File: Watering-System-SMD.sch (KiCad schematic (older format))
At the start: 21 parts, among them CON1 AVR-ISP-6, J1 Screw_Terminal_1x02, J2 CONN_01X04_MALE, J3 Screw_Terminal_1x04, J4 Screw_Terminal_1x02, Q1 MMBF170, Q2 2N7002, U1 MCP1703A-3302/MB, U2 ATTINY84-20SSU, U3 ESP-01

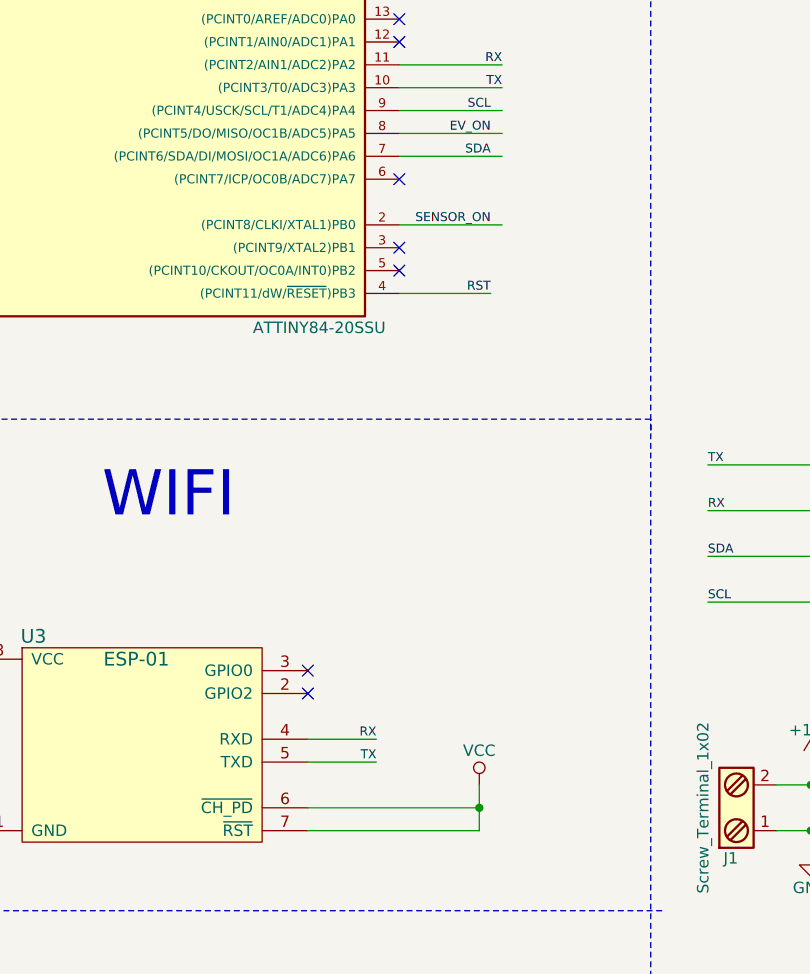
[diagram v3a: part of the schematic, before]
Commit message: CH-PD routed
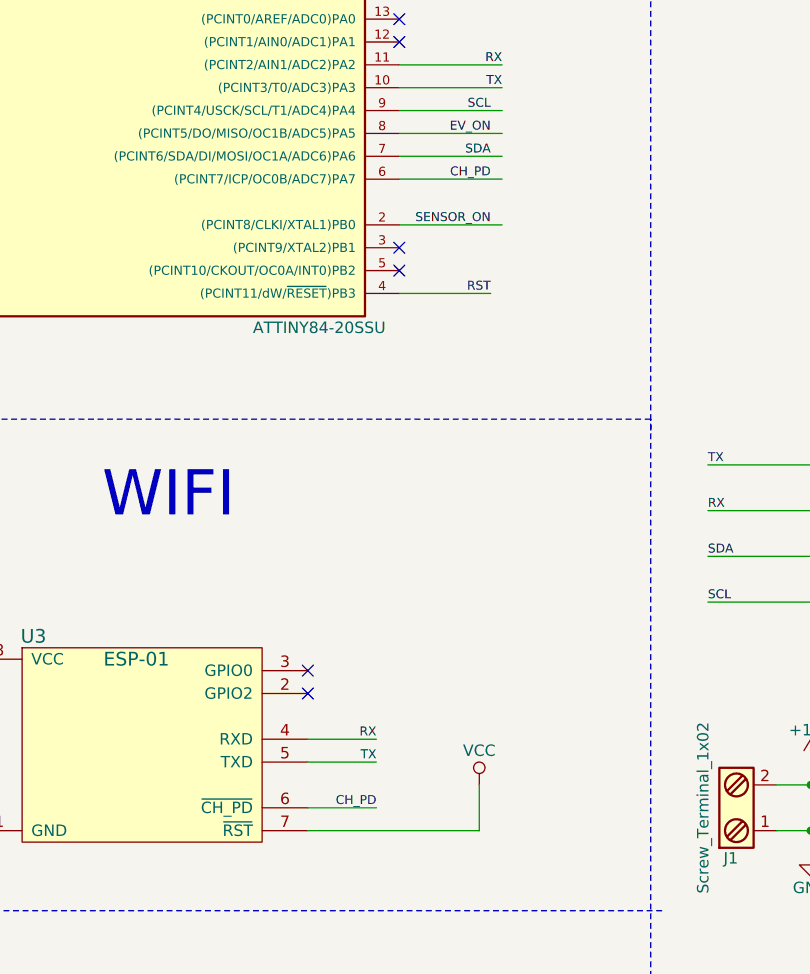
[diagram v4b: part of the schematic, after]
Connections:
- net labels added: CH_PD
- wire segments 78 -> 79
- no-connect marks 7 -> 6
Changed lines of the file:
@@
 Text Label 7000 1400 2    39   ~ 0
 RX
-NoConn ~ 6550 1900
 NoConn ~ 6550 2200
 NoConn ~ 6550 2300
@@
 	6150 4450 6450 4450
 Wire Wire Line
-	6150 4650 6900 4650
-Wire Wire Line
 	6900 4550 6900 4750
 Wire Wire Line
 	6900 4750 6150 4750
-Connection ~ 6900 4650
 $Comp
 L VCC #PWR021
@@
 Wire Wire Line
 	4600 4750 4600 4850
+Wire Wire Line
+	6150 4650 6450 4650
+Wire Wire Line
+	6550 1900 7000 1900
+Text Label 6950 1900 2    39   ~ 0
+CH_PD
+Text Label 6450 4650 2    39   ~ 0
+CH_PD
 $EndSCHEMATC

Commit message: MOSFET transistor changed
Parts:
- Q1: symbol MMBF170 -> MMBF170-RESCUE-Watering-System-SMD
- Q2: symbol 2N7002 -> 2N7002-RESCUE-Watering-System-SMD
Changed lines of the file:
@@
 EESchema Schematic File Version 2
+LIBS:Watering-System-SMD-rescue
 LIBS:power
 LIBS:device
@@
 $EndComp
 $Comp
-L MMBF170 Q1
+L MMBF170-RESCUE-Watering-System-SMD Q1
 U 1 1 5923371B
 P 2650 6950
@@
 $EndComp
 $Comp
-L 2N7002 Q2
+L 2N7002-RESCUE-Watering-System-SMD Q2
 U 1 1 592337CE
 P 5300 6800

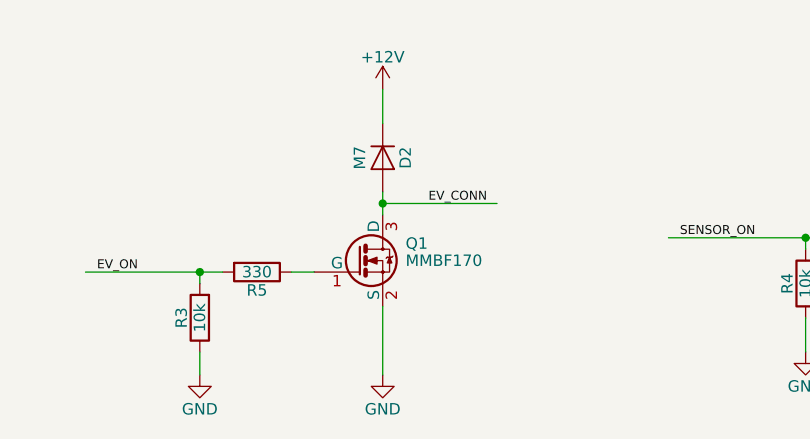
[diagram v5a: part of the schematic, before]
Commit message: MOSFET changed
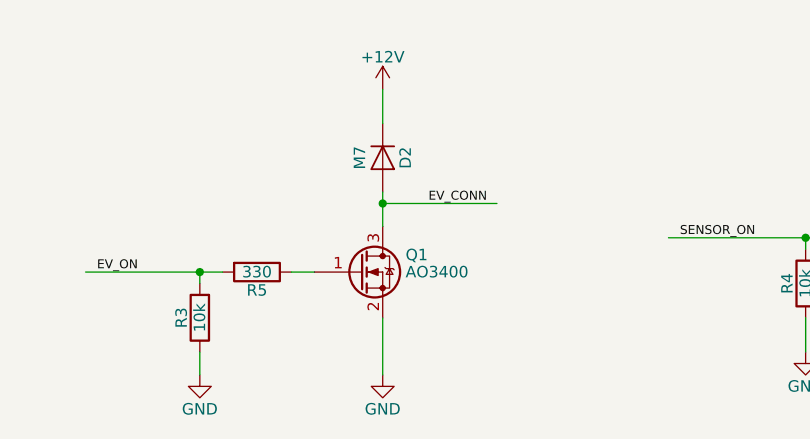
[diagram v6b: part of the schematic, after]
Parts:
- removed Q1: MMBF170, TO_SOT_Packages_SMD:SOT-23, symbol MMBF170-RESCUE-Watering-System-SMD
- added Q1: AO3400, TO_SOT_Packages_SMD:SOT-23, symbol AO3400
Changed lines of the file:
@@
-$EndComp
-$Comp
-L MMBF170-RESCUE-Watering-System-SMD Q1
-U 1 1 5923371B
-P 2650 6950
-F 0 "Q1" H 2850 7025 50  0000 L CNN
-F 1 "MMBF170" H 2850 6950 50  0000 L CNN
-F 2 "TO_SOT_Packages_SMD:SOT-23" H 2850 6875 50  0001 L CIN
-F 3 "" H 2650 6950 50  0001 L CNN
-	1    2650 6950
-	1    0    0    -1
 $EndComp
 $Comp
@@
 Wire Wire Line
 	1950 7350 1950 7450
-Wire Wire Line
-	2750 7150 2750 7450
 Connection ~ 1950 7000
 Wire Wire Line
-	2750 6650 2750 6750
+	2750 6650 2750 6800
 Wire Wire Line
 	2750 6200 2750 6350
@@
 Text Label 6450 4650 2    39   ~ 0
 CH_PD
+$Comp
+L AO3400 Q1
+U 1 1 59E79292
+P 2650 7000
+F 0 "Q1" H 2850 7075 50  0000 L CNN
+F 1 "AO3400" H 2850 7000 50  0000 L CNN
+F 2 "TO_SOT_Packages_SMD:SOT-23" H 2850 6925 50  0001 L CIN
+F 3 "" H 2650 7000 50  0001 L CNN
+	1    2650 7000
+	1    0    0    -1
+$EndComp
+Wire Wire Line
+	2750 7200 2750 7450
 $EndSCHEMATC
